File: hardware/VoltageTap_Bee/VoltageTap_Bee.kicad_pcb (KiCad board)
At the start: 2 copper layers, 138.2 x 105 mm, 159 parts, among them J101 VT, J102 HRLV daisy A, J103 HRLV daisy B, J104 Conn_02x05_Odd_Even, J105 uart, Q201 SiSA96DN, Q202 SiSA96DN, Q203 SiSA96DN, Q204 SiSA96DN, Q205 SiSA96DN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

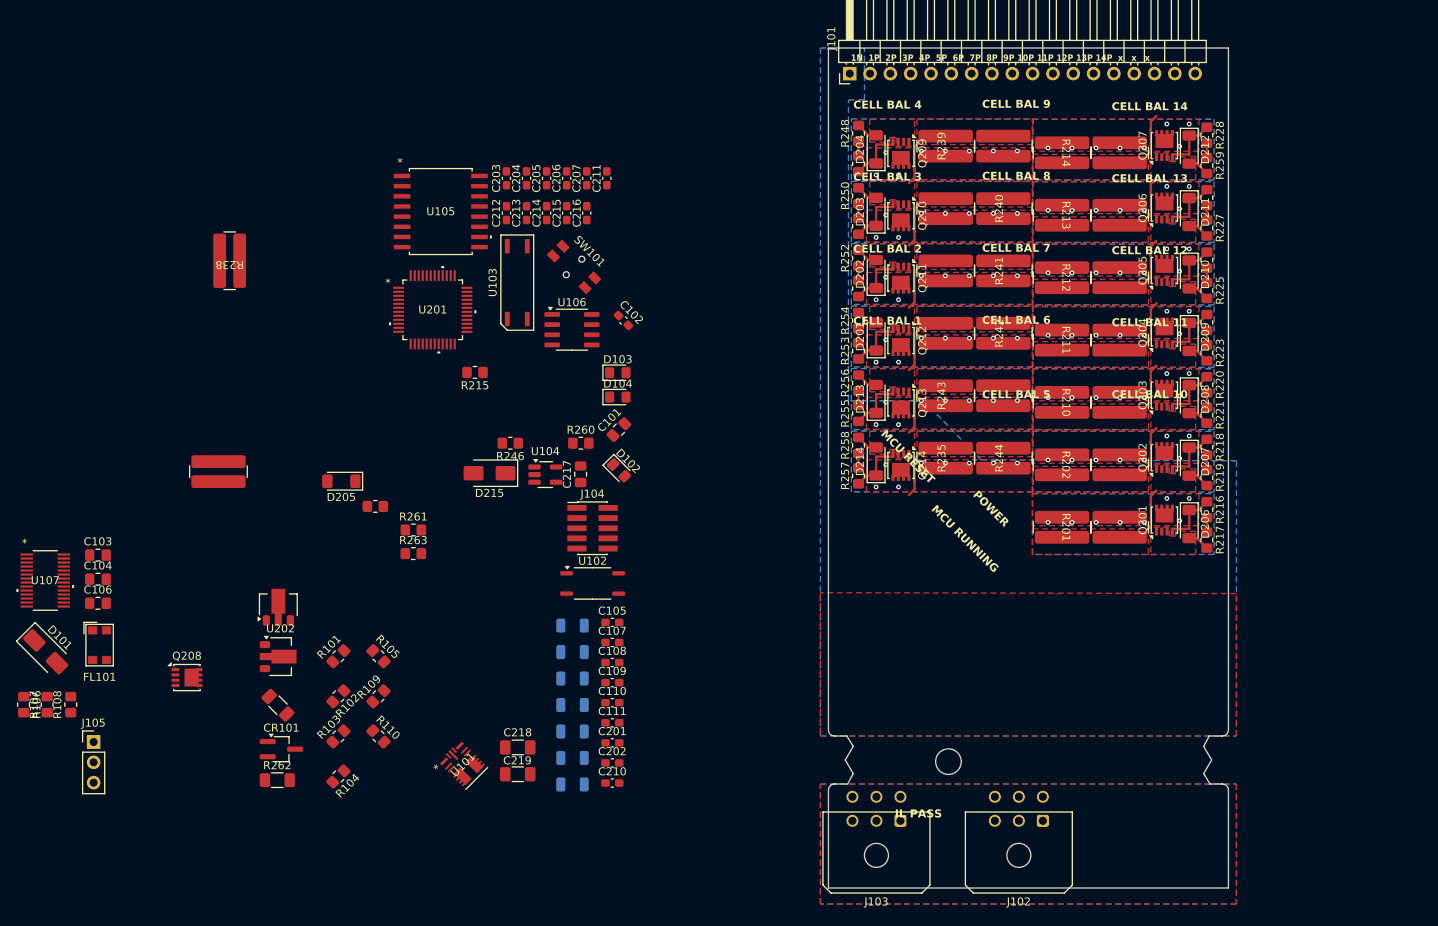
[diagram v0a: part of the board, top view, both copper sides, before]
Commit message: layout update: cell bal and daisy pins
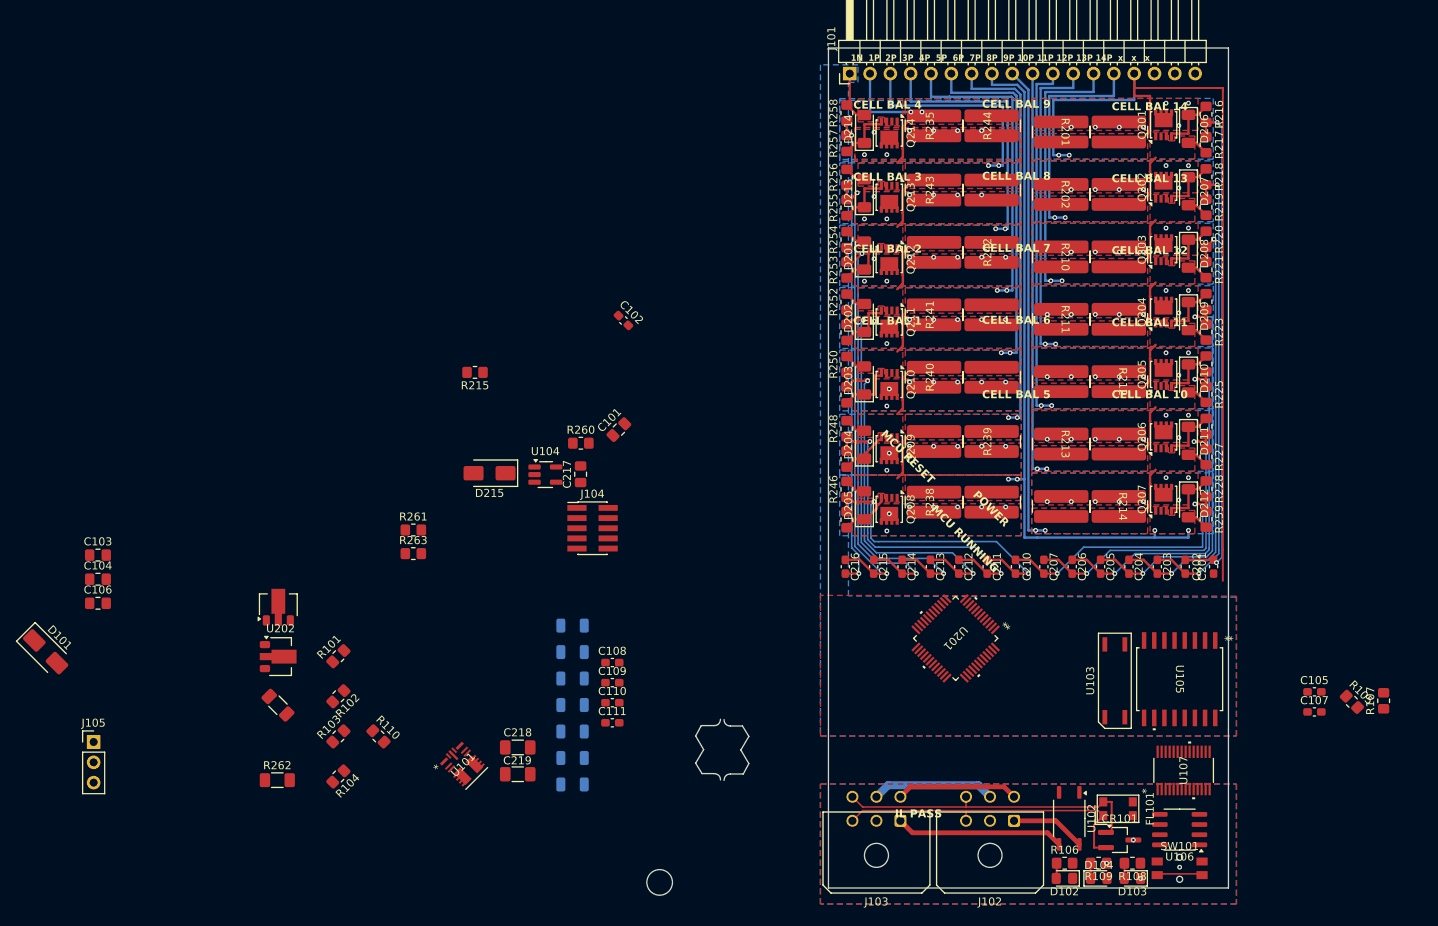
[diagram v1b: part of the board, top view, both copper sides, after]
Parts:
- moved R107 167.1 mm to (189.4, 112.6)
- moved U107 144.3 mm to (164.4, 121.3), turned to 90 degrees
- moved R108 134.2 mm to (158.0, 132.9), turned to 180 degrees
- moved R106 131.6 mm to (149.5, 132.9), turned to 0 degrees
- moved FL101 128.9 mm to (156.2, 126.1), turned to 90 degrees
- moved R105 121.8 mm to (185.4, 112.7)
- moved U105 109.3 mm to (163.9, 109.9), turned to -90 degrees
- moved CR101 105.4 mm to (156.4, 130.0)
- moved SW101 105.3 mm to (163.9, 131.6), turned to 0 degrees
- moved U106 98.4 mm to (163.9, 128.7), turned to 180 degrees
- moved R229 96.7 mm to (140.4, 87.8), turned to 90 degrees
- moved C203 94.7 mm to (161.1, 95.8), turned to -90 degrees
- moved R238 93.1 mm to (133.2, 87.8), turned to 90 degrees
- moved R109 92.4 mm to (153.8, 132.9), turned to 180 degrees
- moved Q208 90.3 mm to (127.6, 88.7), turned to -90 degrees
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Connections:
- C212 pad 2: Net-(C212-Pad2) -> Net-(U201-VC4)
- C213 pad 1: Net-(C212-Pad2) -> Net-(U201-VC4)
- C213 pad 2: Net-(C213-Pad2) -> Net-(U201-VC3)
- C214 pad 1: Net-(C213-Pad2) -> Net-(U201-VC3)
- C214 pad 2: Net-(C214-Pad2) -> Net-(U201-VC2)
- C215 pad 1: Net-(C214-Pad2) -> Net-(U201-VC2)
- CR101 pad 1: /CAN_L -> /CAN+
- CR101 pad 2: /CAN_H -> /CAN-
- FL101 pad 1: /CAN_H -> /CAN-
- FL101 pad 2: Net-(U106-CANH) -> Net-(U106-CANL)
- FL101 pad 3: Net-(U106-CANL) -> Net-(U106-CANH)
- FL101 pad 4: /CAN_L -> /CAN+
- J102 pad 1: /IL+ -> /IL_A+
- J102 pad 3: /CAN_L -> /CAN-
- J102 pad 4: /IL- -> /IL_A-
- J102 pad 6: /CAN_H -> /CAN+
- J103 pad 1: /IL- -> /IL_B+
- J103 pad 3: /CAN_L -> /CAN-
- J103 pad 4: /IL+ -> /IL_A-
- J103 pad 6: /CAN_H -> /CAN+
- U102 pad 4: /IL+ -> /IL_B+
- U102 pad 6: /IL- -> /IL_A+
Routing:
- net +BATT: track 9.35 -> 110.5 mm, vias 0 -> 2
- net /BQ76952 1/7P: track 2.72 -> 88.6 mm, vias 0 -> 4
- net Net-(U201-VC13): track 1.80 -> 62.8 mm, vias 0 -> 2
- net /BQ76952 1/8P: track 12.1 -> 72.1 mm, vias 0 -> 2
- net Net-(U201-VC0): track 1.80 -> 59.3 mm, vias 0 -> 2
- net Net-(U201-VC1): track 1.80 -> 59.1 mm, vias 0 -> 2
- net Net-(U201-VC12): track 1.80 -> 58.8 mm, vias 0 -> 2
- net Net-(U201-VC2): track 1.80 -> 55.5 mm, vias 0 -> 2
- net Net-(U201-VC11): track 1.80 -> 55.1 mm, vias 0 -> 2
- net /BQ76952 1/6P: track 9.35 -> 62.3 mm, vias 0 -> 2
- net /BQ76952 1/9P: track 12.1 -> 63.2 mm, vias 0 -> 2
- net Net-(U201-VC10): track 1.80 -> 51.4 mm, vias 0 -> 2
- net Net-(U201-VC3): track 1.80 -> 49.9 mm, vias 0 -> 2
- net /BQ76952 1/10P: track 12.1 -> 57.5 mm, vias 0 -> 2
- net /BQ76952 1/5P: track 12.1 -> 56.8 mm, vias 0 -> 2
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- added copper zone on B.Cu, net /BQ76952 1/C7Jc
- added copper zone on F.Cu, net /BQ76952 1/C7Jc
- added copper zone on B.Cu, net GND
- added copper zone on F.Cu, net GND
- removed copper zone on B.Cu, net (none)
- removed copper zone on F.Cu, net (none)
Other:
- board size 138.2 x 105 mm -> 154.9 x 105 mm

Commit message: bee
wee
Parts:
- removed R260: 100, Resistor_SMD:R_0805_2012Metric_Pad1.20x1.40mm_HandSolder
- removed TH101, TH102, TH103, TH104, TH105, TH106: Thermistor, Resistor_SMD:R_1206_3216Metric
- removed U202: FCX495, Package_TO_SOT_SMD:SOT-89-3
- added C220: 1u, Capacitor_SMD:C_0603_1608Metric_Pad1.08x0.95mm_HandSolder, F.Cu at (123.3, 104.1)
- added G***: LOGO, LOGO, B.Cu at (128.1, 104.2)
- added REF**: Symbol_HighVoltage_Triangle_6x6mm_Copper, Symbol:Symbol_HighVoltage_Triangle_6x6mm_Copper, F.Cu at (147.8, 100.8)
- added REF**: Symbol_HighVoltage_Triangle_6x6mm_Copper, Symbol:Symbol_HighVoltage_Triangle_6x6mm_Copper, B.Cu at (135.5, 109.8)
- added REF**: Symbol_HighVoltage_Triangle_6x6mm_Copper, Symbol:Symbol_HighVoltage_Triangle_6x6mm_Copper, B.Cu at (144.6, 43.3)
- C108, C109, R111: moved to B.Cu
- C217: value 22u -> 1u; footprint Capacitor_SMD:C_0805_2012Metric_Pad1.18x1.45mm_HandSolder -> Capacitor_SMD:C_0603_1608Metric_Pad1.08x0.95mm_HandSolder
- C218, C219: footprint Capacitor_SMD:C_1206_3216Metric_Pad1.33x1.80mm_HandSolder -> Capacitor_SMD:C_0603_1608Metric_Pad1.08x0.95mm_HandSolder
- TH107: moved to F.Cu
- moved C106 140.2 mm to (165.7, 130.1)
- moved J105 139.6 mm to (167.7, 119.7), turned to 180 degrees
- moved C103 115.8 mm to (140.2, 125.5), turned to -90 degrees
- moved R111 114.7 mm to (165.1, 126.4), turned to -90 degrees
- moved C104 113.0 mm to (138.2, 125.5), turned to -90 degrees
- moved R110 105.3 mm to (168.8, 123.7), turned to -90 degrees
- moved D101 103.6 mm to (123.8, 126.7), turned to 180 degrees
- moved R215 96.5 mm to (168.2, 99.5), turned to -90 degrees
- moved R262 92.2 mm to (141.4, 104.0)
- moved C218 88.3 mm to (168.4, 104.7), turned to -90 degrees
- moved D215 87.7 mm to (163.7, 101.0), turned to 0 degrees
- moved C219 87.4 mm to (166.9, 104.7), turned to -90 degrees
- moved U203 87.4 mm to (138.1, 110.3), turned to 45 degrees
- moved R261 74.2 mm to (140.8, 106.1)
- moved C102 73.8 mm to (136.4, 125.7), turned to 90 degrees
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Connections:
- D215 pad 1: Net-(D215-K) -> /BQ76952 1/BAT
- R101 pad 1: /BQ76952 1/HDQ -> /BQ76952 1/CFETOFF
- R102 pad 1: /BQ76952 1/CFETOFF -> /BQ76952 1/HDQ
- R107 pad 2: PA15_BBQ_RESET -> /bbqrst
- R261 pad 2: Net-(D215-K) -> /BQ76952 1/BAT
- R262 pad 1: Net-(D215-K) -> /BQ76952 1/BAT
- U105 pad 3: PA18_SPI1_MOSI -> /bbqCS
- U105 pad 4: PB14_BBQ_CS -> PA18_SPI1_MOSI
- U107 pad 10: /led.sched -> unconnected-(U107-PA3_/_LFXIN-Pad10)
- U107 pad 11: /IL EN -> unconnected-(U107-PA4_/_LFCLK_IN_/_LFXOUT-Pad11)
- U107 pad 14: unconnected-(U107-PA9_/_RTC_OUT_/_CLK_OUT-Pad14) -> /led.sched
- U107 pad 17: PB14_BBQ_CS -> unconnected-(U107-PA14/CLK_OUT/A0_12-Pad17)
- U107 pad 18: PA15_BBQ_RESET -> unconnected-(U107-PA15/A1_0-Pad18)
- U107 pad 24: unconnected-(U107-PA21/A1_7/VREF--Pad24) -> /bbqCS
- U107 pad 27: unconnected-(U107-PA24/A0_3-Pad27) -> /bbqrst
- U107 pad 28: unconnected-(U107-PA25/A0_2-Pad28) -> /IL EN
- U201 pad 1: +BATT -> Net-(U201-VC14)
- U201 pad 48: +BATT -> Net-(U201-VC14)
- U203 pad 2: Net-(D215-K) -> /BQ76952 1/BAT
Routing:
- net +3.3V: track 0.00 -> 54.1 mm, vias 0 -> 2
- net /BQ76952 1/BAT: track 0.00 -> 50.3 mm
- net +5V: track 0.00 -> 47.8 mm
- net Net-(U105-OUTC): track 0.00 -> 44.2 mm, vias 0 -> 2
- net Net-(U105-IND): track 0.00 -> 44.1 mm, vias 0 -> 2
- net /BQ0_3.3v: track 0.00 -> 40.8 mm
- net Net-(U201-VC14): track 0.00 -> 38.7 mm
- net Net-(U105-OUTB): track 0.00 -> 37.6 mm, vias 0 -> 2
- net Net-(U201-VC13): track 62.8 -> 98.9 mm
- net /BQ76952 1/RST_SHUT: track 0.00 -> 35.1 mm, vias 0 -> 2
- net Net-(U105-OUTA): track 0.00 -> 34.2 mm, vias 0 -> 2
- net Net-(U201-VC12): track 58.8 -> 90.6 mm
- net Net-(U201-VC11): track 55.1 -> 83.6 mm
- net /MCU_RESET: track 5.73 -> 33.7 mm, vias 0 -> 2
- net Net-(U201-VC10): track 51.4 -> 76.6 mm
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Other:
- board size 154.9 x 105 mm -> 50 x 110.1 mm
- board text added: "<->"
- board text added: "GND"
- board text added: "High Voltage"
- board text added: "Low Voltage"
- board text added: "RX"
- board text added: "TX"
- board text added: "Voltage Tap Bee 3.0 github.com/Gregification/BeeMS/ 3/23/2026 - pinning & hardware info: {dblquote}/hardware/VoltageTap_Bee/{dblquote} - indirect cell taps - 14 cells. cells 14,15,16 internaly joined"
- board text added: "cell 1"
- board text added: "cell 10"
- board text added: "cell 11"
- board text added: "cell 12"
- board text added: "cell 13"
- board text added: "cell 14"
- board text added: "cell 2"
- board text added: "cell 3"
- board text added: "cell 4"
- board text added: "cell 5"
- board text added: "cell 6"
- board text added: "cell 7"
- board text added: "cell 8"
- board text added: "cell 9"
- board text added: "tty 118200 8N1"
- board text removed: "3V3 UART RX UART TX GND"
- board text removed: "CELL BAL 1"
- board text removed: "CELL BAL 10"
- board text removed: "CELL BAL 11"
- board text removed: "CELL BAL 12"
- board text removed: "CELL BAL 13"
- board text removed: "CELL BAL 14"
- board text removed: "CELL BAL 2"
- board text removed: "CELL BAL 3"
- board text removed: "CELL BAL 4"
- board text removed: "CELL BAL 5"
- board text removed: "CELL BAL 6"
- board text removed: "CELL BAL 7"
- board text removed: "CELL BAL 8"
- board text removed: "CELL BAL 9"
- board text removed: "GLV"
- board text removed: "GND 3V3 UART RX UART TX SWDIO SWCLK"
- board text removed: "HV"
- board text removed: "IL PASS"
- board text removed: "MCU RESET"
- board text removed: "MCU RUNNING"
- board text removed: "POWER"
- board text removed: "Voltage Tap Bee github.com/Gregification/BeeMS/ 2/25/2026 - pinning & hardware info: {dblquote}/hardware/VoltageTap_Bee/{dblquote} - indirect cell taps - 14 cells. cells 14,15,16 internaly joined"

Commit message: ordered
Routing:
- net +BATT: track 117.0 -> 116.0 mm
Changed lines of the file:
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@@
 			(drillshape 0)
 			(scaleselection 1)
-			(outputdirectory "./Gerber")
+			(outputdirectory "C:/Users/turtl/Downloads/jlc/")
 		)
 	)
@@
 		)
 		(fp_line
-			(start 4.5974 -0.6103)
-			(end 4.5974 -0.889699)
+			(start -0.6103 4.5974)
+			(end -0.610301 3.594101)
 			(stroke
 				(width 0.0254)
@@
 		)
 		(fp_line
-			(start -0.6103 4.5974)
-			(end -0.610301 3.594101)
+			(start 4.5974 -0.6103)
+			(end 4.5974 -0.889699)
 			(stroke
 				(width 0.0254)
@@
 		)
 		(fp_line
-			(start 4.5974 -0.889699)
-			(end 3.5941 -0.889699)
+			(start -0.889699 4.5974)
+			(end -0.6103 4.5974)
 			(stroke
 				(width 0.0254)
@@
 		)
 		(fp_line
-			(start -0.889699 4.5974)
-			(end -0.6103 4.5974)
+			(start 4.5974 -0.889699)
+			(end 3.5941 -0.889699)
 			(stroke
 				(width 0.0254)
@@
 		)
 		(fp_line
-			(start 0.889699 -4.5974)
-			(end 0.6103 -4.5974)
+			(start -4.5974 0.889699)
+			(end -3.5941 0.889699)
 			(stroke
 				(width 0.0254)
@@
 		)
 		(fp_line
-			(start -4.5974 0.889699)
-			(end -3.5941 0.889699)
+			(start 0.889699 -4.5974)
+			(end 0.6103 -4.5974)
 			(stroke
 				(width 0.0254)
@@
 		)
 		(fp_line
-			(start 0.6103 -4.5974)
-			(end 0.610301 -3.594101)
+			(start -4.5974 0.6103)
+			(end -4.5974 0.889699)
 			(stroke
 				(width 0.0254)
@@
 		)
 		(fp_line
-			(start -4.5974 0.6103)
-			(end -4.5974 0.889699)
+			(start 0.6103 -4.5974)
+			(end 0.610301 -3.594101)
 			(stroke
 				(width 0.0254)
@@
 			)
 			(layer "F.SilkS")
-			(net 1198542451)
 		)
 		(fp_line
@@
 			)
 			(layer "F.SilkS")
-			(net 1198542451)
 		)
 		(fp_line
@@
 			)
 			(layer "F.SilkS")
-			(net 1198542451)
 		)
 		(fp_line
@@
 			)
 			(layer "F.SilkS")
-			(net 1198542451)
 		)
 		(fp_line
@@
 			)
 			(layer "F.SilkS")
-			(net 1198542451)
 		)
 		(fp_line
@@
 			)
 			(layer "F.SilkS")
-			(net 1198542451)
 		)
 		(fp_line
@@
 			)
 			(layer "F.SilkS")
-			(net 1198542451)
 		)
 		(fp_line
@@
 			)
 			(layer "F.SilkS")
-			(net 1198542451)
 		)
 		(fp_line
@@
 			)
 			(layer "F.SilkS")
-			(net 1198542451)
 		)
 		(fp_poly
@@
 			(fill yes)
 			(layer "F.SilkS")
-			(net 1198542451)
 		)
 		(embedded_fonts no)
@@
 	)
 	(segment
-		(start 158.219999 36)
-		(end 158.219999 34.200001)
-		(width 0.25)
+		(start 160.199999 41.400001)
+		(end 160.2 38.700002)
+		(width 0.3)
 		(layer "F.Cu")
 		(net 32)
 	)
 	(segment
-		(start 160.199999 41.400001)
-		(end 160.2 38.700002)
-		(width 0.3)
+		(start 158.219999 34.200001)
+		(end 160.019998 36)
+		(width 0.25)
 		(layer "F.Cu")
 		(net 32)
@@
 	)
 	(segment
-		(start 169.3 100.1)
-		(end 169.3 36)
-		(width 0.25)
-		(layer "F.Cu")
-		(net 32)
-	)
-	(segment
 		(start 168.2 100.500001)
 		(end 168.9 100.500001)
@@
 	)
 	(segment
-		(start 169.3 36)
-		(end 158.219999 36)
-		(width 0.25)
-		(layer "F.Cu")
-		(net 32)
-	)
-	(segment
 		(start 168.9 100.500001)
 		(end 169.3 100.1)
@@
 		(layer "F.Cu")
 		(net 32)
+	)
+	(segment
+		(start 169.3 36)
+		(end 169.3 100.1)
+		(width 0.25)
+		(layer "F.Cu")
+		(net 32)
+	)
+	(segment
+		(start 160.019998 36)
+		(end 169.3 36)
+		(width 0.25)
+		(layer "F.Cu")
+		(net 32)
